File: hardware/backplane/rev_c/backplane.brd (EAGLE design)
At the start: 254 x 381 mm, 379 parts, among them J0 BACKPLANE_GENERIC_MODULE, J1 BACKPLANE_GENERIC_MODULE, J2 BACKPLANE_GENERIC_MODULE, J3 BACKPLANE_CONTROLLER_MODULE, J4 BACKPLANE_POWER_MODULE, J5 BACKPLANE_GENERIC_MODULE, J6 BACKPLANE_GENERIC_MODULE, J7 BACKPLANE_GENERIC_MODULE, U1 TUSB2077A, U10 SN74LVC2T45, U11 SN74LVC2T45, U12 SN74LVC2T45, U13 SN74LVC2T45, U14 SN74LVC2T45, U15 SN74LVC2T45, U16 SN74LVC2T45, U17 SN74LVC2T45, U18 SN74LVC2T45, U19 SN74LVC2T45, U2 FXMA2102, U20 TS3USB30E, U21 TS3USB30E, U22 TS3USB30E, U23 TS3USB30E, U24 TS3USB30E, U25 TS3USB30E, U26 MCP23008QFN, U27 MCP23008QFN, U28 MCP23008QFN, U29 MCP23008QFN, U3 FXMA2102, U30 MCP23008QFN, U31 MCP23008QFN, U32 MCP23008QFN, U4 FXMA2102, U5 FXMA2102, U6 FXMA2102, U7 FXMA2102, U8 SN74LVC2T45, U9 SN74LVC2T45, Y1 ABMM

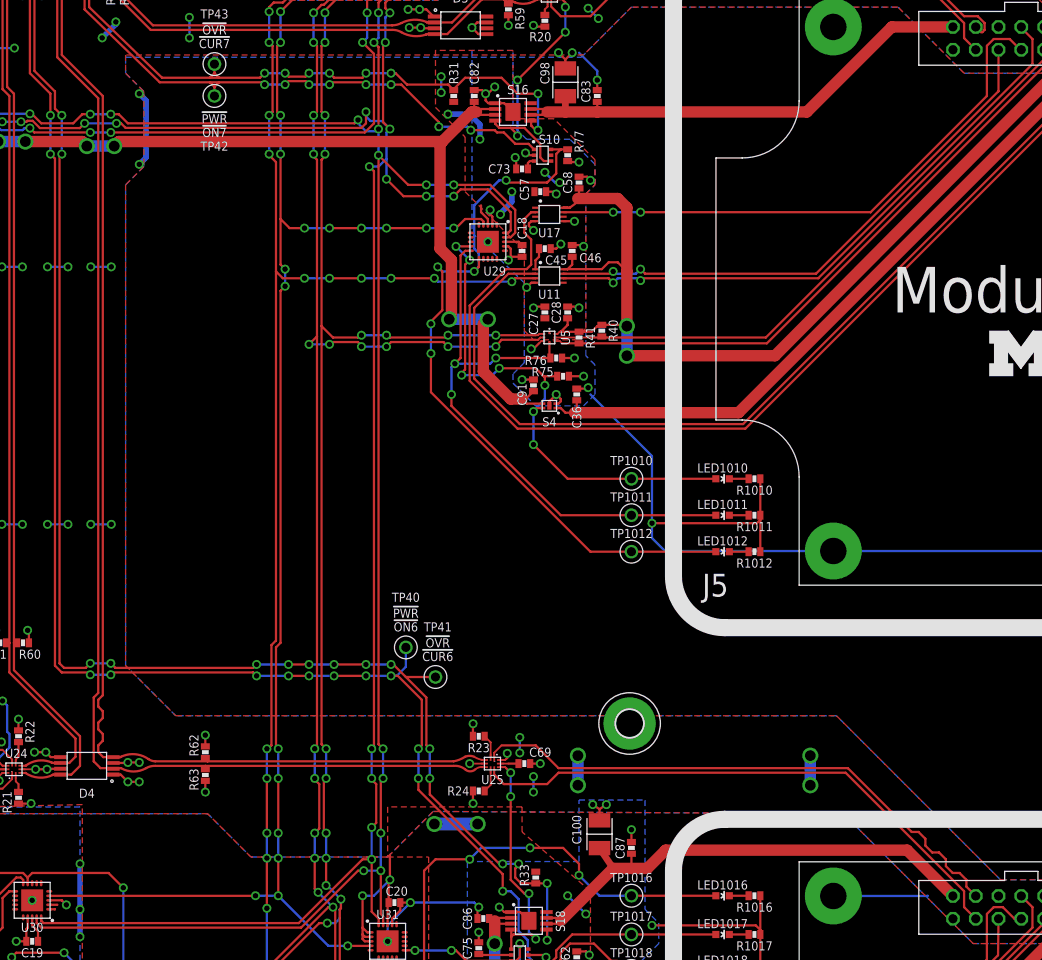
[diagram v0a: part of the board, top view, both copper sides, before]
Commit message: backplane: clean up MOD7 USB traces a bit
MOD7 USB didn't work on one board. I didn't actually debug that
board, but may as well clean these up while we're doing things.
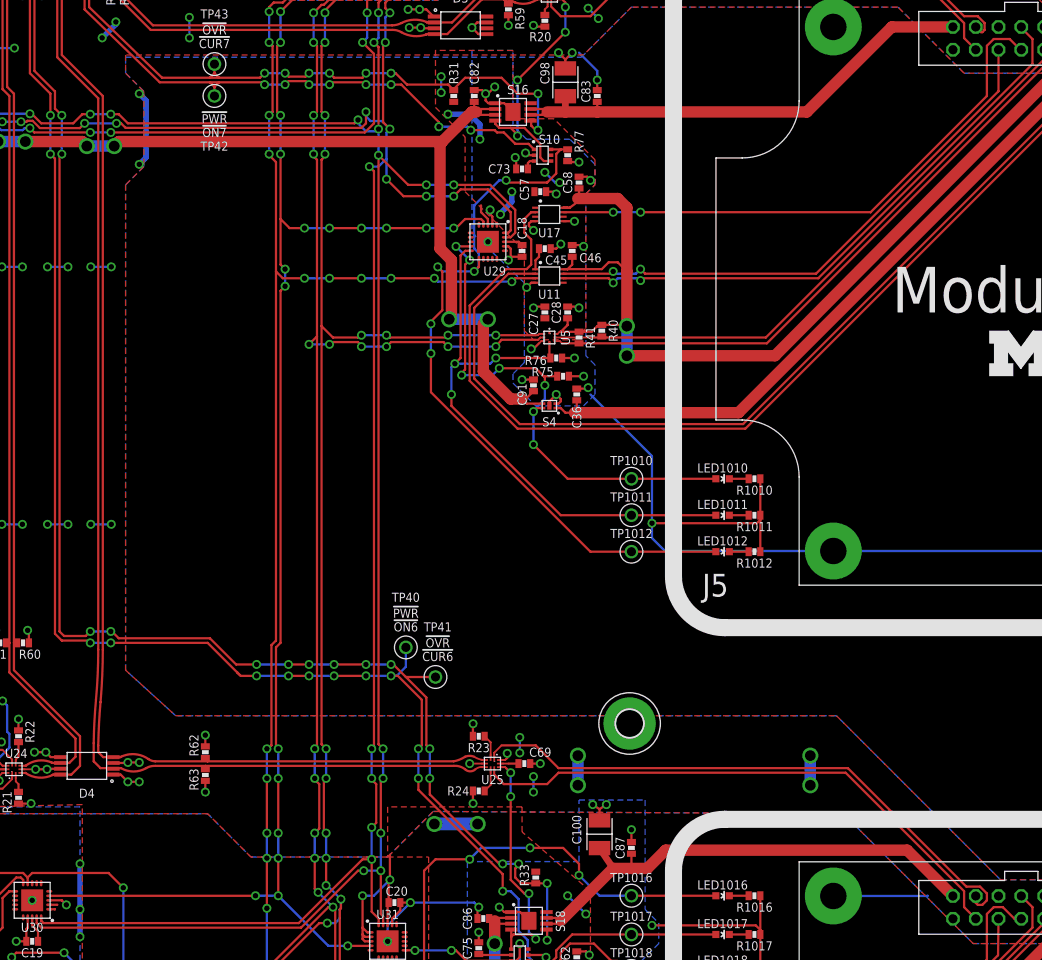
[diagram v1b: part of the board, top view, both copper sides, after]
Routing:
- net MOD7_USB+: track 62.9 -> 65.8 mm
- net HUB_!OVRCUR6: track 184.8 -> 182.4 mm
- net HUB_!PWRON6: track 221.6 -> 219.6 mm
- net MOD7_D+_HUB-SW: track 145.0 -> 143.9 mm

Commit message: backplane: move all traces away from board edges
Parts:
- moved JP2 1.05 mm to (238.8, 11.7)
- moved JP1 0.72 mm to (13.2, 14.7)
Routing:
- net VCC_LINUX: track 701.1 -> 443.6 mm, vias 9 -> 1
- net CONT_MOD6_IN: track 516.6 -> 401.6 mm
- net CONT_MOD6_OUT: track 515.4 -> 401.2 mm
- net VCC_CONTROLLER: track 789.9 -> 744.1 mm
- net MOD7_5V_METERED: track 475.4 -> 448.4 mm
- net MOD1_5V_METERED: track 457.9 -> 451.2 mm
- net CONT_MOD7_OUT: track 373.1 -> 367.4 mm
- net CONT_MOD7_IN: track 357.3 -> 351.6 mm
- net CONT_MOD5_OUT: track 272.7 -> 267.2 mm
- net MOD6_5V_METERED: track 172.3 -> 167.1 mm
- net CONT_MOD5_IN: track 265.8 -> 261.5 mm
- net HUB_!PWRON4: track 289.4 -> 285.7 mm, vias 7 -> 6
- net HUB_!OVRCUR4: track 237.0 -> 234.0 mm
- net GND: track 2944.8 -> 2942.5 mm

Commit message: backplane: replace USB caps with shorter package
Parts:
- C100, C95, C96, C97, C98, C99: device passives:1210_CAP -> resistor:C1206
- moved C100 1.08 mm to (161.5, 80.5), turned to 90 degrees
- moved C96 1.05 mm to (160.8, 360.4), turned to 90 degrees
- moved C99 0.80 mm to (41.7, 89.7), turned to 0 degrees
- moved C97 0.57 mm to (36.3, 283.2), turned to 180 degrees
- moved C95 0.57 mm to (95.0, 327.7), turned to 90 degrees
- moved C98 0.57 mm to (157.5, 164.8), turned to 90 degrees
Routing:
- net MOD0_USB_VBUS: track 91.7 -> 90.3 mm

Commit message: backplane: bump rev on silkscreen
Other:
- board text added: "2017-03-07"
- board text added: "Rev C. 2017-03-07"
- board text added: "RevC"
- board text removed: "Rev B. 2016-09-21"
- board text removed: "RevB 2016-09-21"

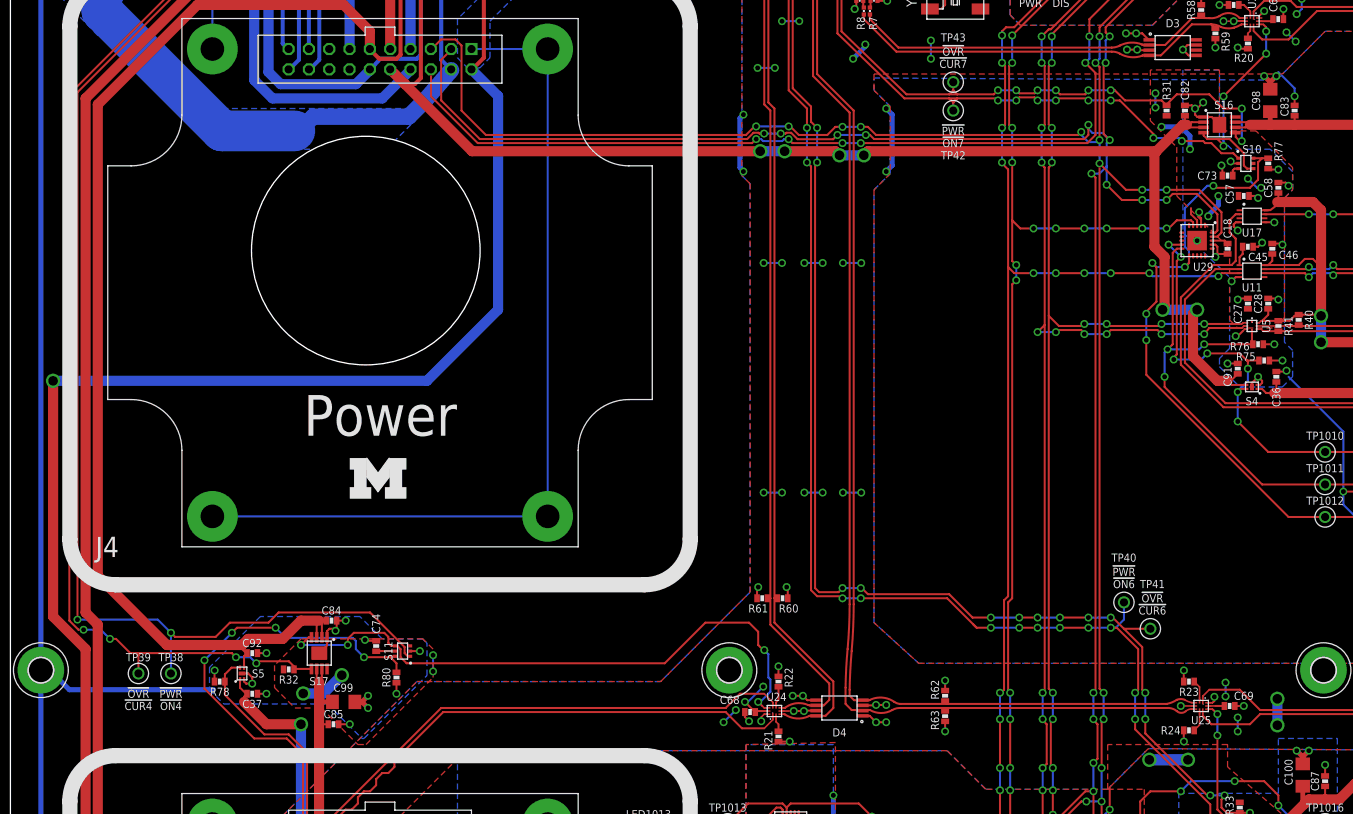
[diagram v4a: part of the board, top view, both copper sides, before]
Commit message: added slot for waterproof entries
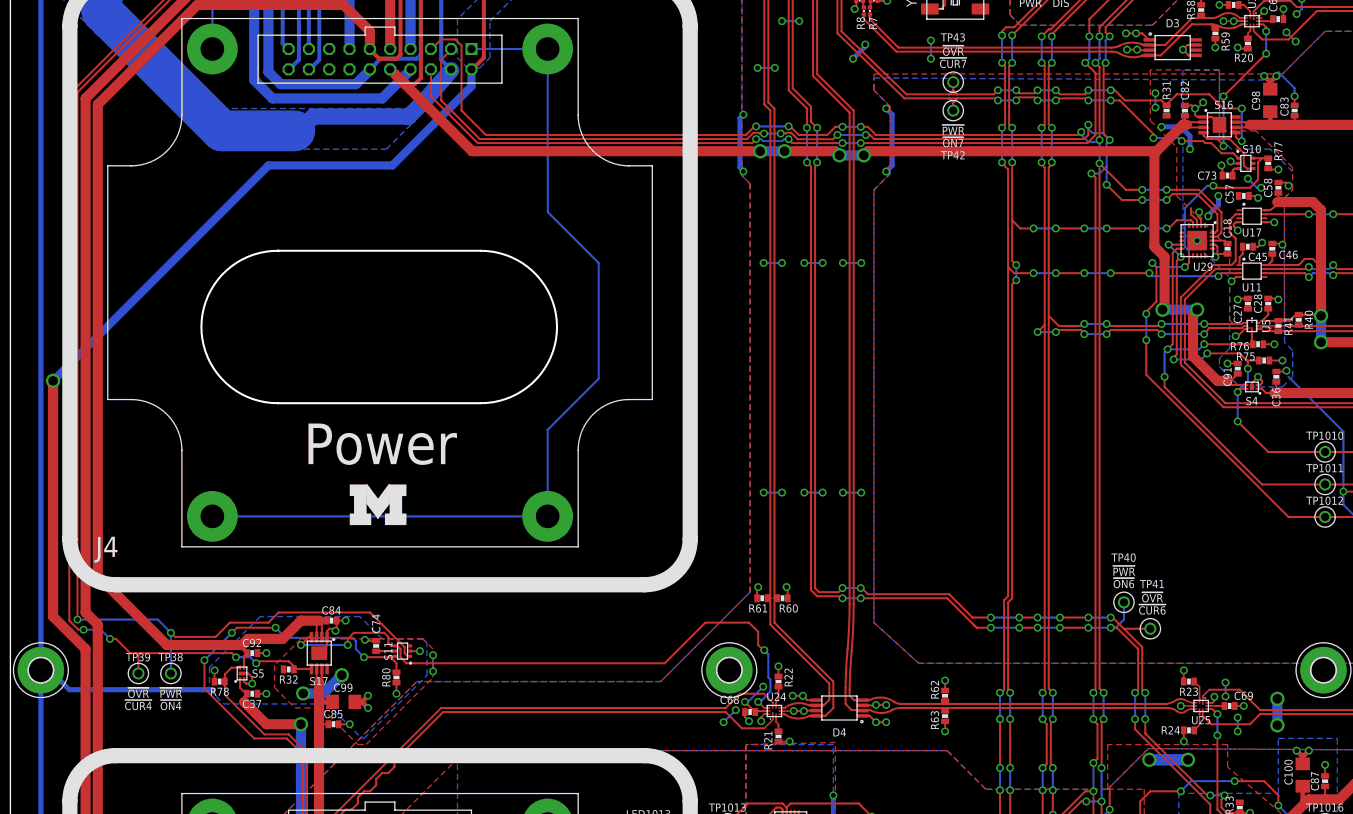
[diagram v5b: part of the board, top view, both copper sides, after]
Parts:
- moved LOGO9 3.30 mm to (42.4, 111.8)
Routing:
- net VCC_CONTROLLER: track 744.1 -> 723.0 mm
- net GND: track 2942.0 -> 2946.4 mm
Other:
- outline, holes or cut-outs redrawn
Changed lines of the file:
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@@
 <?xml version="1.0" encoding="utf-8"?>
 <!DOCTYPE eagle SYSTEM "eagle.dtd">
-<eagle version="8.0.2">
+<eagle version="6.6.0">
 <drawing>
 <settings>
@@
 <setting verticaltext="up"/>
 </settings>
-<grid distance="10" unitdist="mil" unit="mil" style="lines" multiple="1" display="yes" altdistance="5" altunitdist="mil" altunit="mil"/>
+<grid distance="0.005" unitdist="inch" unit="inch" style="lines" multiple="1" display="yes" altdistance="0.01" altunitdist="inch" altunit="inch"/>
 <layers>
 <layer number="1" name="Top" color="4" fill="1" visible="yes" active="yes"/>
@@
 <text x="46.228" y="45.212" size="5.08" layer="21" font="vector" ratio="15" align="center">Module 6</text>
 <text x="207.772" y="45.212" size="5.08" layer="21" font="vector" ratio="15" align="center">Module 7</text>
-<text x="46.228" y="125.476" size="5.08" layer="21" font="vector" ratio="15" align="center">Power</text>
+<text x="46.228" y="121.92" size="5.08" layer="21" font="vector" ratio="15" align="center">Power</text>
 <text x="207.772" y="238.76" size="5.08" layer="21" font="vector" ratio="15" align="center">Control</text>
 <text x="218.694" y="208.534" size="1.016" layer="21" font="vector" ratio="12" align="center-left">RevC</text>
-<hole x="44.4246" y="146.0754" drill="28.575"/>
 <text x="127.508" y="188.214" size="1.016" layer="21" font="vector" ratio="20" align="bottom-center">HUB
 CFG</text>
@@
 </polygon>
 <text x="218.694" y="207.264" size="0.762" layer="21" font="vector" ratio="12" align="center-left">2017-03-07</text>
+<wire x1="33.401" y1="146.05" x2="33.528" y2="146.05" width="0.254" layer="20"/>
+<wire x1="33.528" y1="146.05" x2="58.801" y2="146.05" width="0.254" layer="20"/>
+<wire x1="33.401" y1="127" x2="58.801" y2="127" width="0.254" layer="20"/>
+<wire x1="33.401" y1="127" x2="33.528" y2="146.05" width="0.254" layer="20" curve="-180.763898"/>
+<wire x1="58.801" y1="146.05" x2="58.801" y2="127" width="0.254" layer="20" curve="-180"/>
 </plain>
 <attributes>
@@
 <pass name="Default">
 <param name="RoutingGrid" value="50mil"/>
-<param name="AutoGrid" value="1"/>
-<param name="Efforts" value="0"/>
-<param name="TopRouterVariant" value="1"/>
 <param name="tpViaShape" value="round"/>
 <param name="PrefDir.1" value="|"/>
@@
 <element name="LOGO7" library="logos" package="UMICH_SOLID_200MIL" value="UMICH_SOLID_MEDIUM" x="204.47" y="35.814"/>
 <element name="LOGO8" library="logos" package="UMICH_SOLID_200MIL" value="UMICH_SOLID_MEDIUM" x="204.216" y="229.87"/>
-<element name="LOGO9" library="logos" package="UMICH_SOLID_200MIL" value="UMICH_SOLID_MEDIUM" x="42.418" y="115.062"/>
+<element name="LOGO9" library="logos" package="UMICH_SOLID_200MIL" value="UMICH_SOLID_MEDIUM" x="42.418" y="111.76"/>
 <element name="R51" library="passives" package="0603-RES" value="10kΩ" x="105.918" y="191.77" rot="R180"/>
 <element name="JP1" library="SparkFun-Aesthetics" package="FIDUCIAL-1X2" value="FIDUCIAL1X2" x="13.208" y="14.732"/>
@@
 <wire x1="67.1576" y1="192.6844" x2="70.612" y2="189.23" width="0.254" layer="16"/>
 <wire x1="25.2476" y1="112.8522" x2="67.1576" y2="112.8522" width="0.254" layer="16"/>
-<wire x1="67.1576" y1="171.2722" x2="67.1576" y2="112.8522" width="0.254" layer="16"/>
+<wire x1="67.1576" y1="171.2722" x2="67.183" y2="150.876" width="0.254" layer="16"/>
+<wire x1="67.183" y1="150.876" x2="73.533" y2="144.526" width="0.254" layer="16"/>
+<wire x1="73.533" y1="144.526" x2="73.533" y2="130.048" width="0.254" layer="16"/>
+<wire x1="73.533" y1="130.048" x2="67.1576" y2="123.6726" width="0.254" layer="16"/>
+<wire x1="67.1576" y1="123.6726" x2="67.1576" y2="112.8522" width="0.254" layer="16"/>
 <wire x1="228.7524" y1="365.0234" x2="228.7524" y2="306.6034" width="0.254" layer="16"/>
 <contactref element="H17" pad="B3,0"/>
@@
 <via x="160.782" y="83.566" extent="1-16" drill="0.6"/>
 <via x="162.306" y="83.566" extent="1-16" drill="0.6"/>
-<wire x1="161.544" y1="82.804" x2="161.544" y2="81.918" width="0.6096" layer="1"/>
 <wire x1="161.544" y1="82.804" x2="162.306" y2="83.566" width="0.6096" layer="1"/>
 <wire x1="161.544" y1="81.918" x2="161.544" y2="82.804" width="0.6096" layer="1"/>
@@
 <contactref element="J3" pad="2"/>
 <wire x1="57.6326" y1="168.7322" x2="57.6326" y2="168.6306" width="1.27" layer="16"/>
-<wire x1="52.07" y1="129.794" x2="5.334" y2="129.794" width="1.27" layer="16"/>
 <via x="5.334" y="129.794" extent="1-16" drill="1.2"/>
 <wire x1="5.334" y1="100.33" x2="9.398" y2="96.266" width="1.27" layer="1"/>
@@
 <wire x1="65.024" y1="193.04" x2="71.12" y2="193.04" width="0.508" layer="1"/>
 <wire x1="5.334" y1="100.33" x2="5.334" y2="129.794" width="1.27" layer="1"/>
-<wire x1="52.07" y1="129.794" x2="60.96" y2="138.684" width="1.27" layer="16"/>
-<wire x1="60.96" y1="138.684" x2="60.96" y2="165.4048" width="1.27" layer="16"/>
-<wire x1="60.96" y1="165.4048" x2="57.6326" y2="168.7322" width="1.27" layer="16"/>
 <wire x1="13.290440625" y1="9.398" x2="9.398" y2="13.290440625" width="1.27" layer="1" curve="-90"/>
 <wire x1="9.398" y1="13.290440625" x2="9.398" y2="96.266" width="1.27" layer="1"/>
@@
 <wire x1="234.95" y1="195.072" x2="234.95" y2="195.199" width="1.27" layer="16"/>
 <wire x1="234.95" y1="195.199" x2="244.602" y2="185.547" width="1.27" layer="16"/>
+<wire x1="57.6326" y1="168.7322" x2="57.6326" y2="166.5986" width="1.016" layer="16"/>
+<wire x1="57.6326" y1="166.5986" x2="47.752" y2="156.718" width="1.016" layer="16"/>
+<wire x1="47.752" y1="156.718" x2="32.258" y2="156.718" width="1.016" layer="16"/>
+<wire x1="32.258" y1="156.718" x2="5.334" y2="129.794" width="1.016" layer="16"/>
 </signal>
 <signal name="VCC_LINUX">
